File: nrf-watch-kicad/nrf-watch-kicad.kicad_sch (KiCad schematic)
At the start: 90 parts, among them IC1 TLV840MAPL36DBVRQ1, IC2 XC9265C181MR-G, IC3 TPS61023DRLT, IC4 MAX30101EFD+T, M1 Vibrator DC Motor, Q1 DMP2045U-7, Q2 SS8050-G, U1 MAX1811ESA+, U2 DMC2400UV-7, U3 LIS2DS12TR, U4 MX25R6435FZNIL0, U5 u-blox ANNA-B402, U6 DRV2603RUNT, U7 XC9265A331MR-G, U8 TXB0104QRUTRQ1, U9 GC9A01

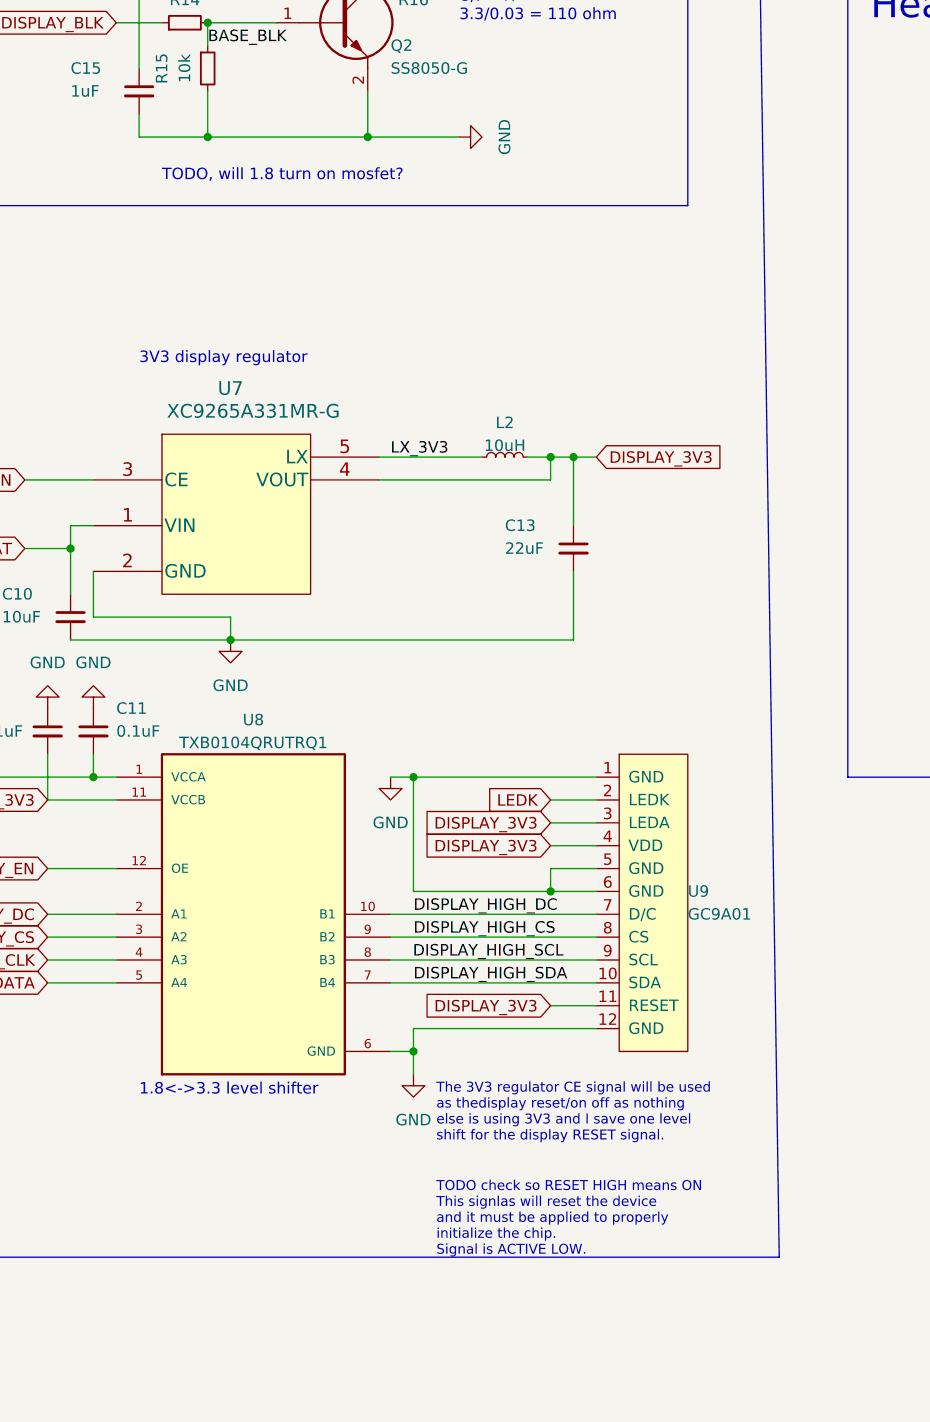
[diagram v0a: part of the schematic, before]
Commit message: Minor estetic changes in sch1ematic.
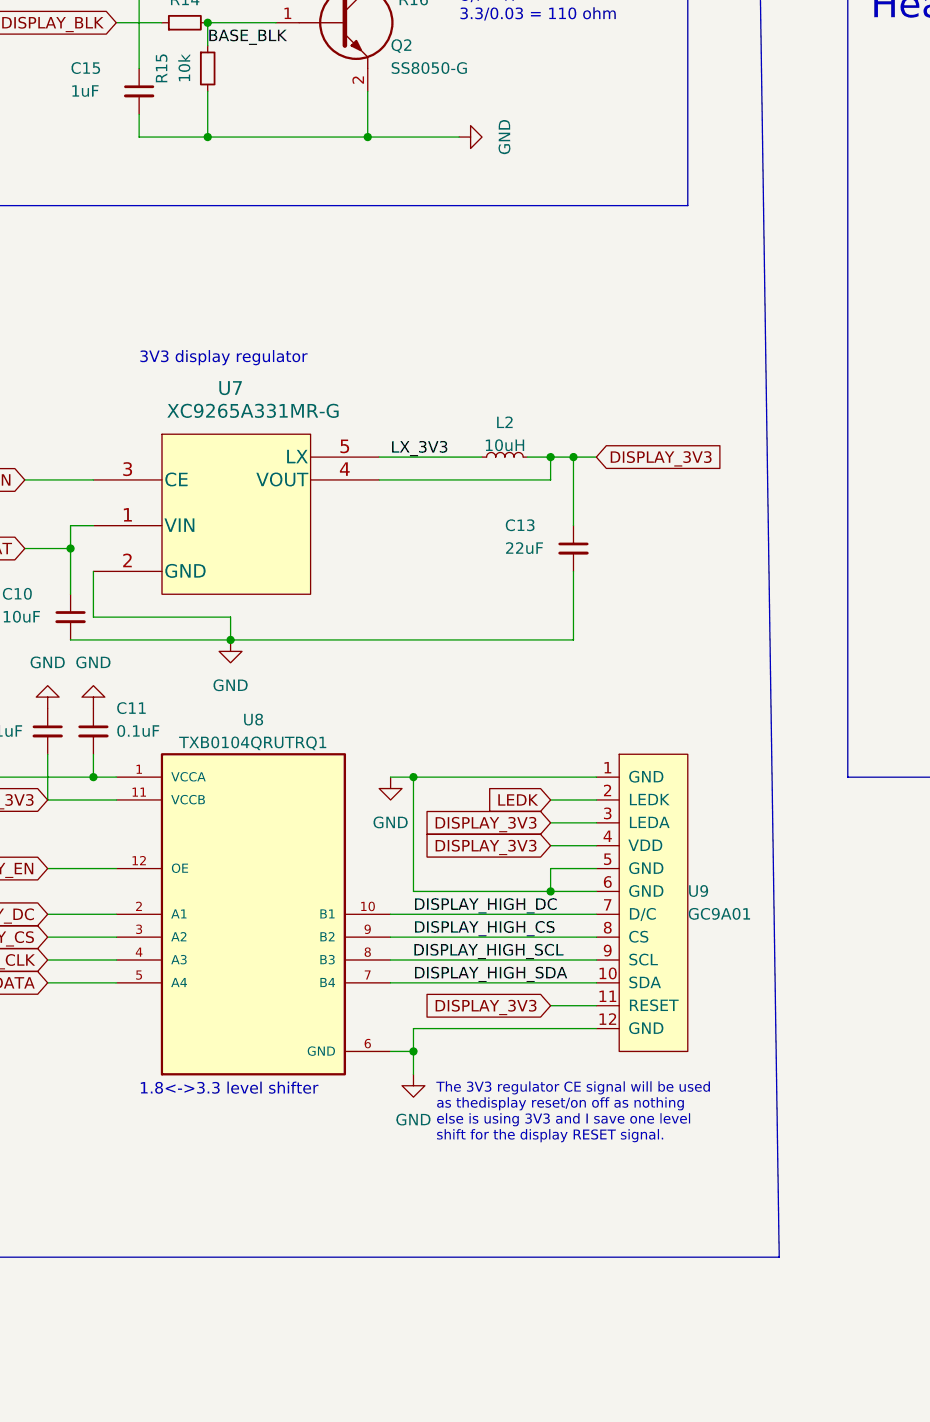
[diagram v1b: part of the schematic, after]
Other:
- note removed: "TODO check so RESET HIGH means ON This signlas will reset the device and it must be applied to properly initialize the chip. Signal is ACTIVE LOW."
- note removed: "TODO, will 1.8 turn on mosfet?"
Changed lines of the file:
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@@
-    (effects (font (size 1.27 1.27)) (justify left bottom))
-  )
-  (text "TODO, will 1.8 turn on mosfet?" (at 203.2 172.72 0)
     (effects (font (size 1.27 1.27)) (justify left bottom))
   )
@@
     (effects (font (size 3 3)) (justify left bottom))
   )
-  (text "TODO check so RESET HIGH means ON\nThis signlas will reset the device\nand it must be applied to properly\ninitialize the chip.\nSignal is ACTIVE LOW."
-    (at 233.68 292.1 0)
-    (effects (font (size 1.1 1.1)) (justify left bottom))
-  )
   (text "Display" (at 175.26 127 0)

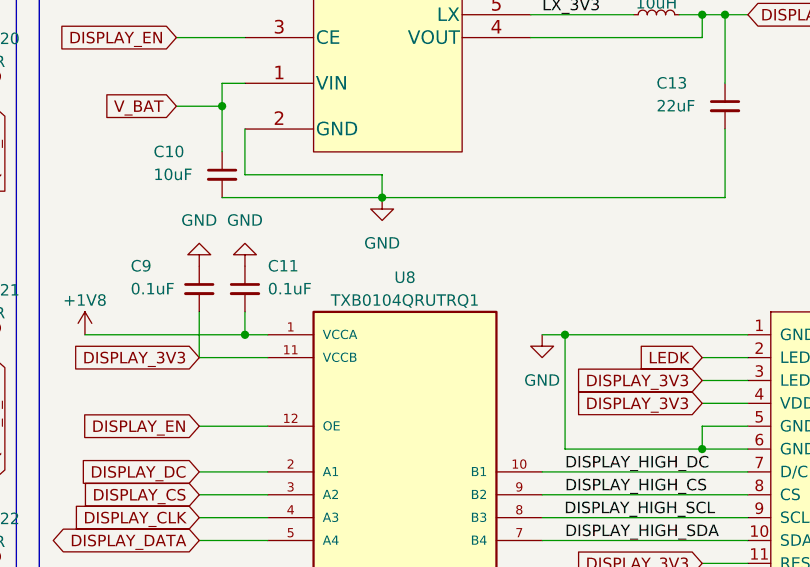
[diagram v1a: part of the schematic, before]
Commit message: Fix pin bug offset in TXB0104QRUTRQ1 footprint.
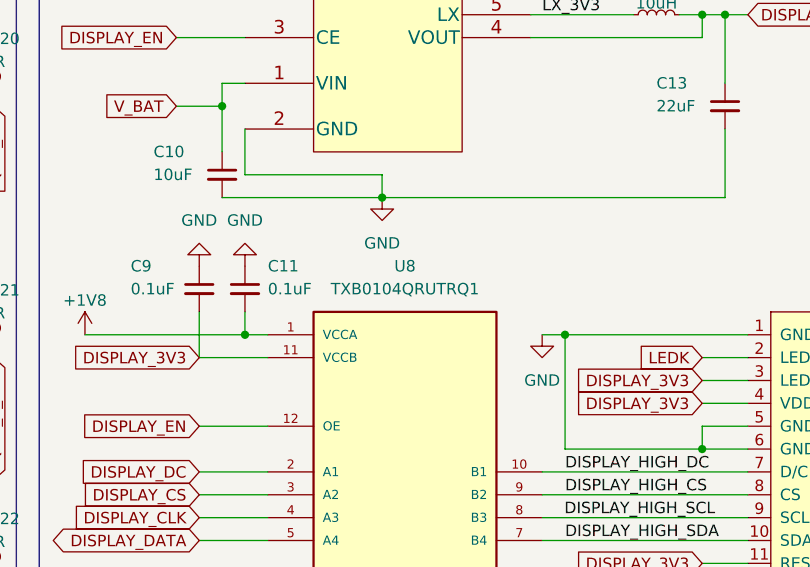
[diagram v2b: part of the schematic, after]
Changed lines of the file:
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@@
   (symbol (lib_id "user_library:TXB0104QRUTRQ1") (at 213.36 254 0) (unit 1)
     (in_bom yes) (on_board yes) (fields_autoplaced)
-    (property "Reference" "U8" (id 0) (at 213.36 232.41 0))
-    (property "Value" "TXB0104QRUTRQ1" (id 1) (at 213.36 234.95 0))
+    (property "Reference" "U8" (id 0) (at 213.36 231.14 0))
+    (property "Value" "TXB0104QRUTRQ1" (id 1) (at 213.36 233.68 0))
     (property "Footprint" "SamacSys_Parts:HPA01164RUTR" (id 2) (at 213.36 254 0)
       (effects (font (size 1.27 1.27)) (justify left bottom) hide)

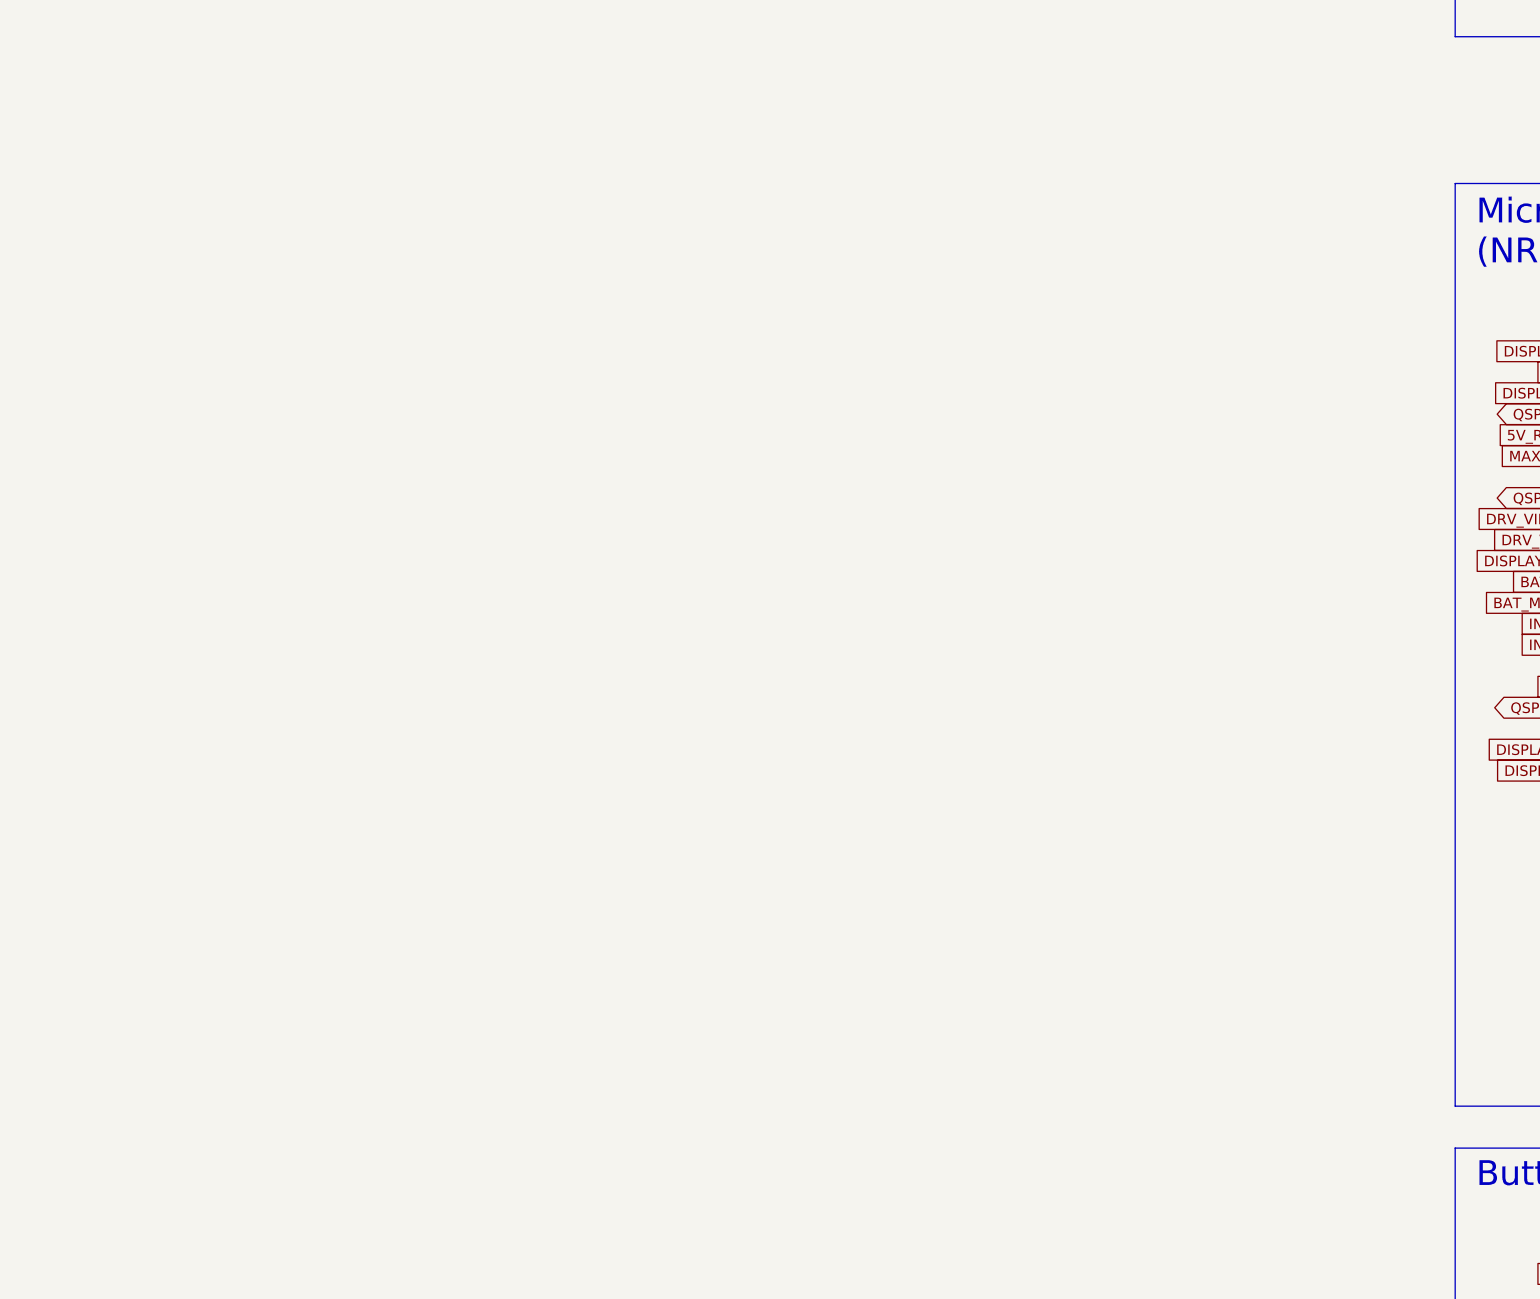
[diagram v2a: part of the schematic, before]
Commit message: Bring in NINA-B406 option fo simpler soldering instead of ANNA.
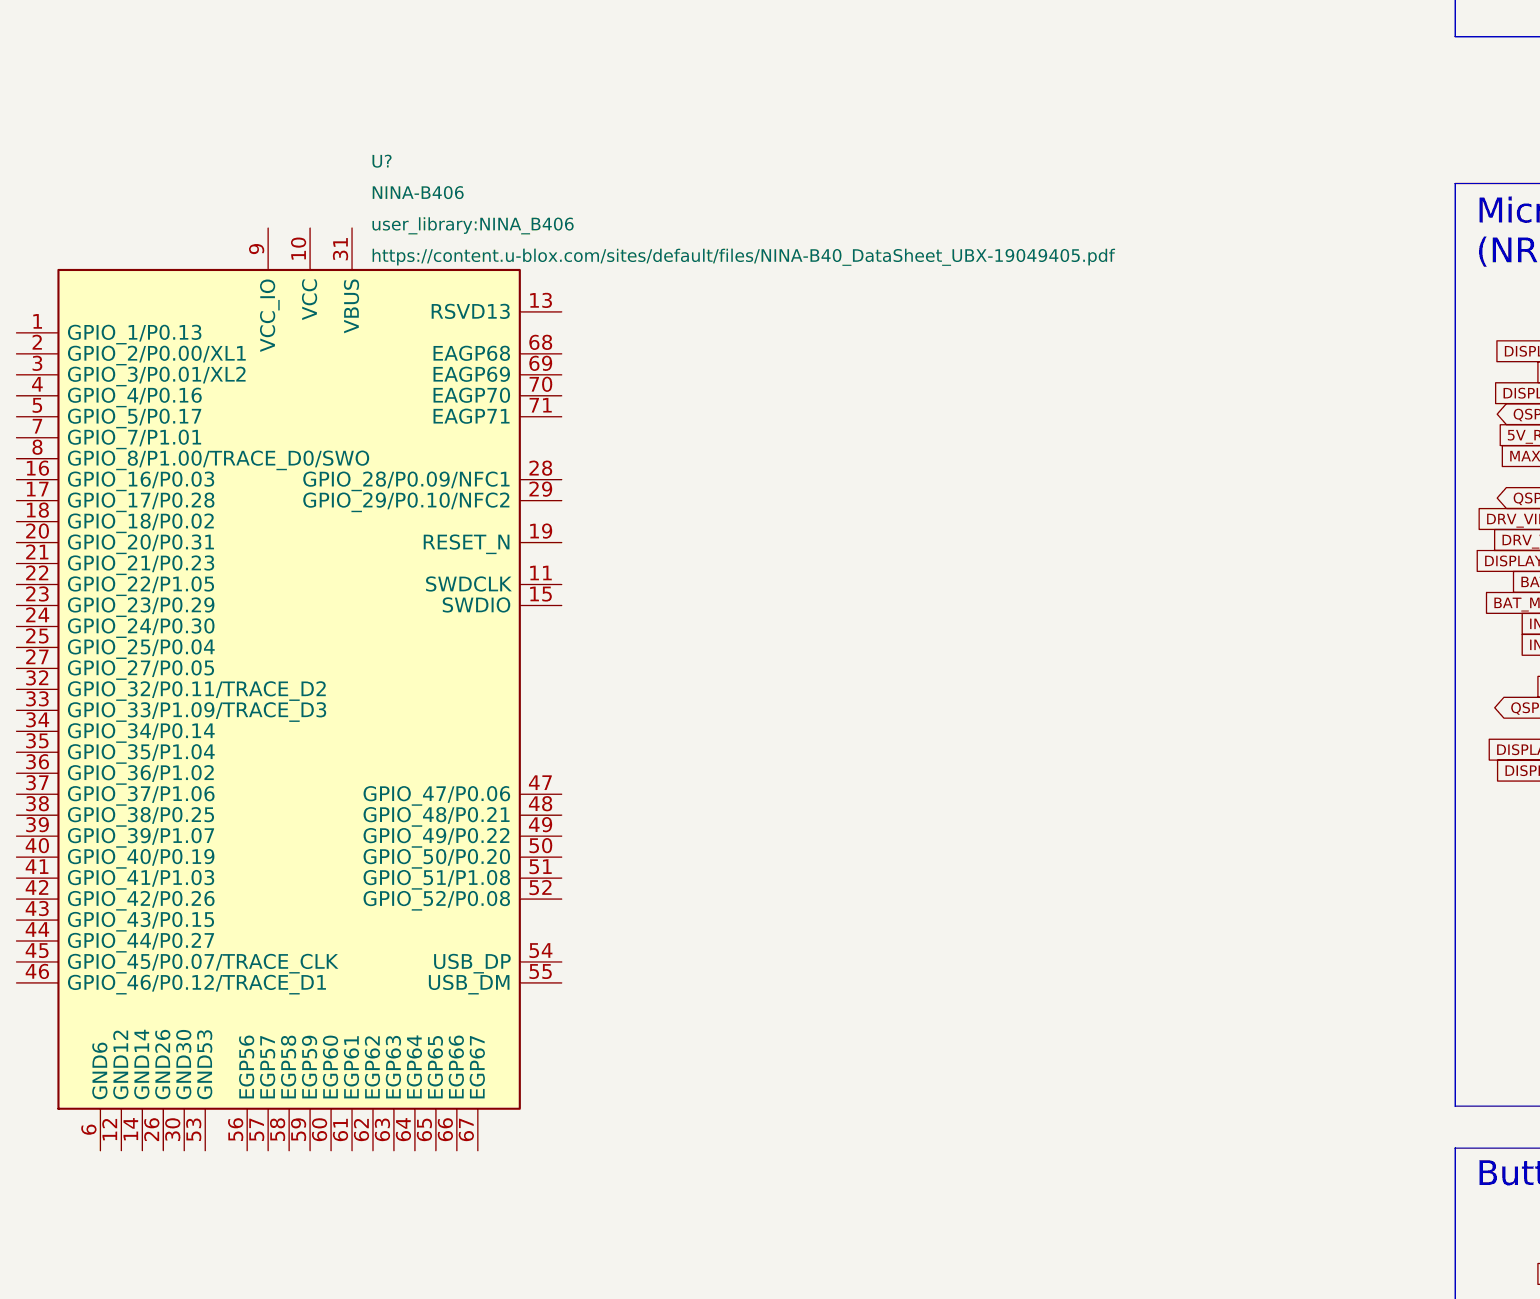
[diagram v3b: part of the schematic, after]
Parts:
- added U?: NINA-B406, user_library:NINA_B406, symbol user_library:NINA-B406
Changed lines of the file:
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@@
     (pin "2")
+  )
+  (symbol (lib_id "user_library:NINA-B406") (at -153.9421 180.655 0) (unit 1)
+    (in_bom yes) (on_board yes) (fields_autoplaced)
+    (property "Reference" "U?" (id 0) (at -116.0833 167.5309 0)
+      (effects (font (size 1.524 1.524)) (justify left))
+    )
+    (property "Value" "NINA-B406" (id 1) (at -116.0833 171.3409 0)
+      (effects (font (size 1.524 1.524)) (justify left))
+    )
+    (property "Footprint" "user_library:NINA_B406" (id 2) (at -116.0833 175.1509 0)
+      (effects (font (size 1.524 1.524)) (justify left))
+    )
+    (property "Datasheet" "https://content.u-blox.com/sites/default/files/NINA-B40_DataSheet_UBX-19049405.pdf" (id 3) (at -116.0833 178.9609 0)
+      (effects (font (size 1.524 1.524)) (justify left))
+    )
+    (pin "1")
+    (pin "10")
+    (pin "11")
+    (pin "12")
+    (pin "13")
+    (pin "14")
+    (pin "15")
+    (pin "16")
+    (pin "17")
+    (pin "18")
+    (pin "19")
+    (pin "2")
+    (pin "20")
+    (pin "21")
+    (pin "22")
+    (pin "23")
+    (pin "24")
+    (pin "25")
+    (pin "26")
+    (pin "27")
+    (pin "28")
+    (pin "29")
+    (pin "3")
+    (pin "30")
+    (pin "31")
+    (pin "32")
+    (pin "33")
+    (pin "34")
+    (pin "35")
+    (pin "36")
+    (pin "37")
+    (pin "38")
+    (pin "39")
+    (pin "4")
+    (pin "40")
+    (pin "41")
+    (pin "42")
+    (pin "43")
+    (pin "44")
+    (pin "45")
+    (pin "46")
+    (pin "47")
+    (pin "48")
+    (pin "49")
+    (pin "5")
+    (pin "50")
+    (pin "51")
+    (pin "52")
+    (pin "53")
+    (pin "54")
+    (pin "55")
+    (pin "56")
+    (pin "57")
+    (pin "58")
+    (pin "59")
+    (pin "6")
+    (pin "60")
+    (pin "61")
+    (pin "62")
+    (pin "63")
+    (pin "64")
+    (pin "65")
+    (pin "66")
+    (pin "67")
+    (pin "68")
+    (pin "69")
+    (pin "7")
+    (pin "70")
+    (pin "71")
+    (pin "8")
+    (pin "9")
   )
   (symbol (lib_id "power:GND") (at 43.18 40.64 0) (unit 1)
@@
       (reference "U9") (unit 1) (value "GC9A01") (footprint "user_library:GC9A01_disp")
     )
-  )
+    (path "/bc223fa1-6d6e-482b-8f2d-79b246ea5c7d"
+      (reference "U?") (unit 1) (value "NINA-B406") (footprint "user_library:NINA_B406")
+    )
+  )
